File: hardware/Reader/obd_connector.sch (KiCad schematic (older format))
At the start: 1 part, among them CN1 AHDF15A-KG-TAXB

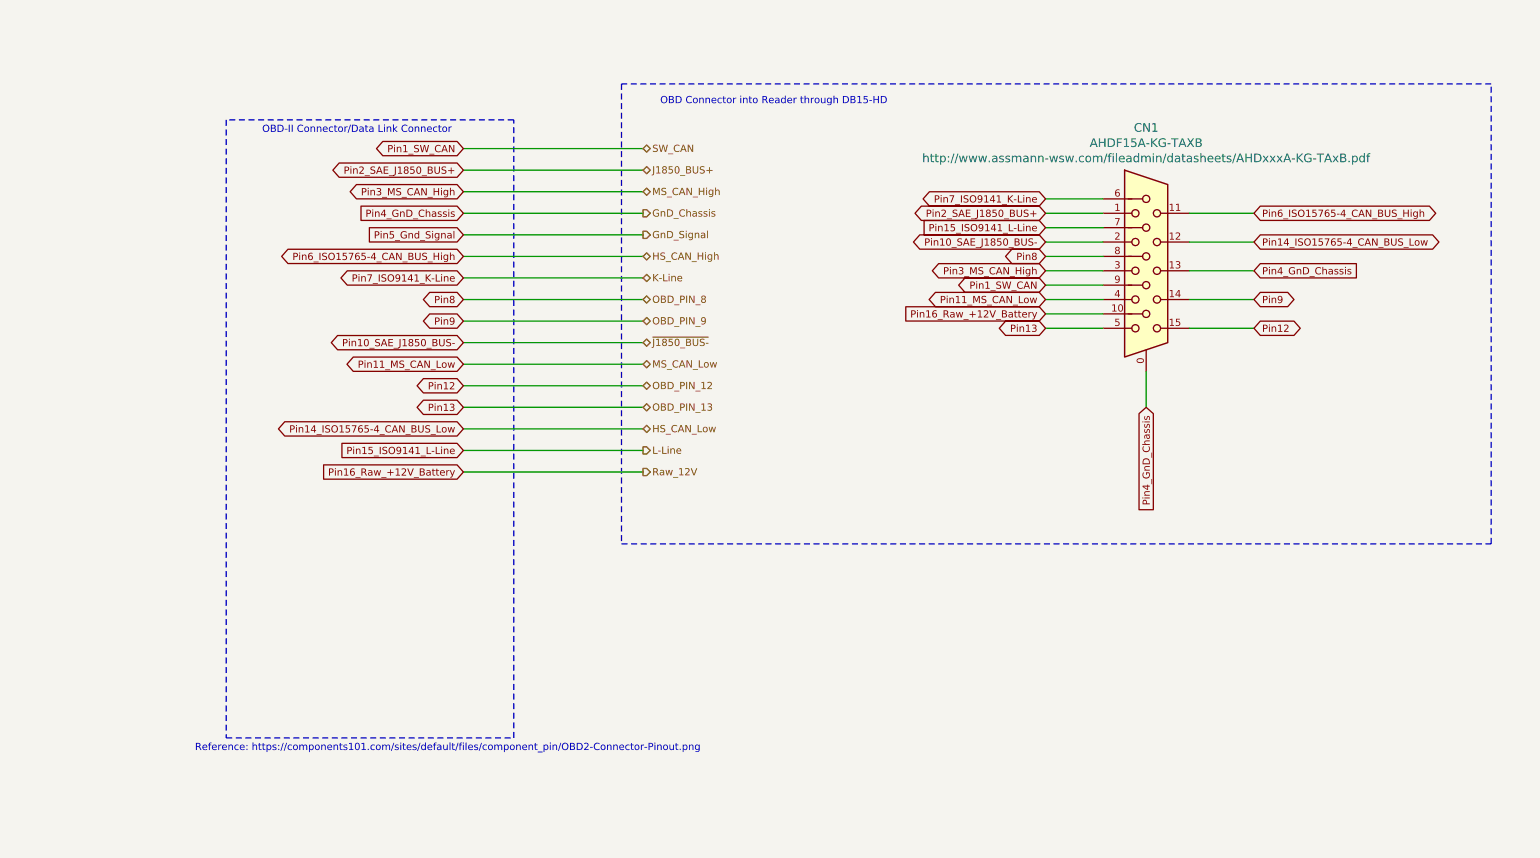
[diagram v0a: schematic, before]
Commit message: Completed Reader schematics for version 0.0.01
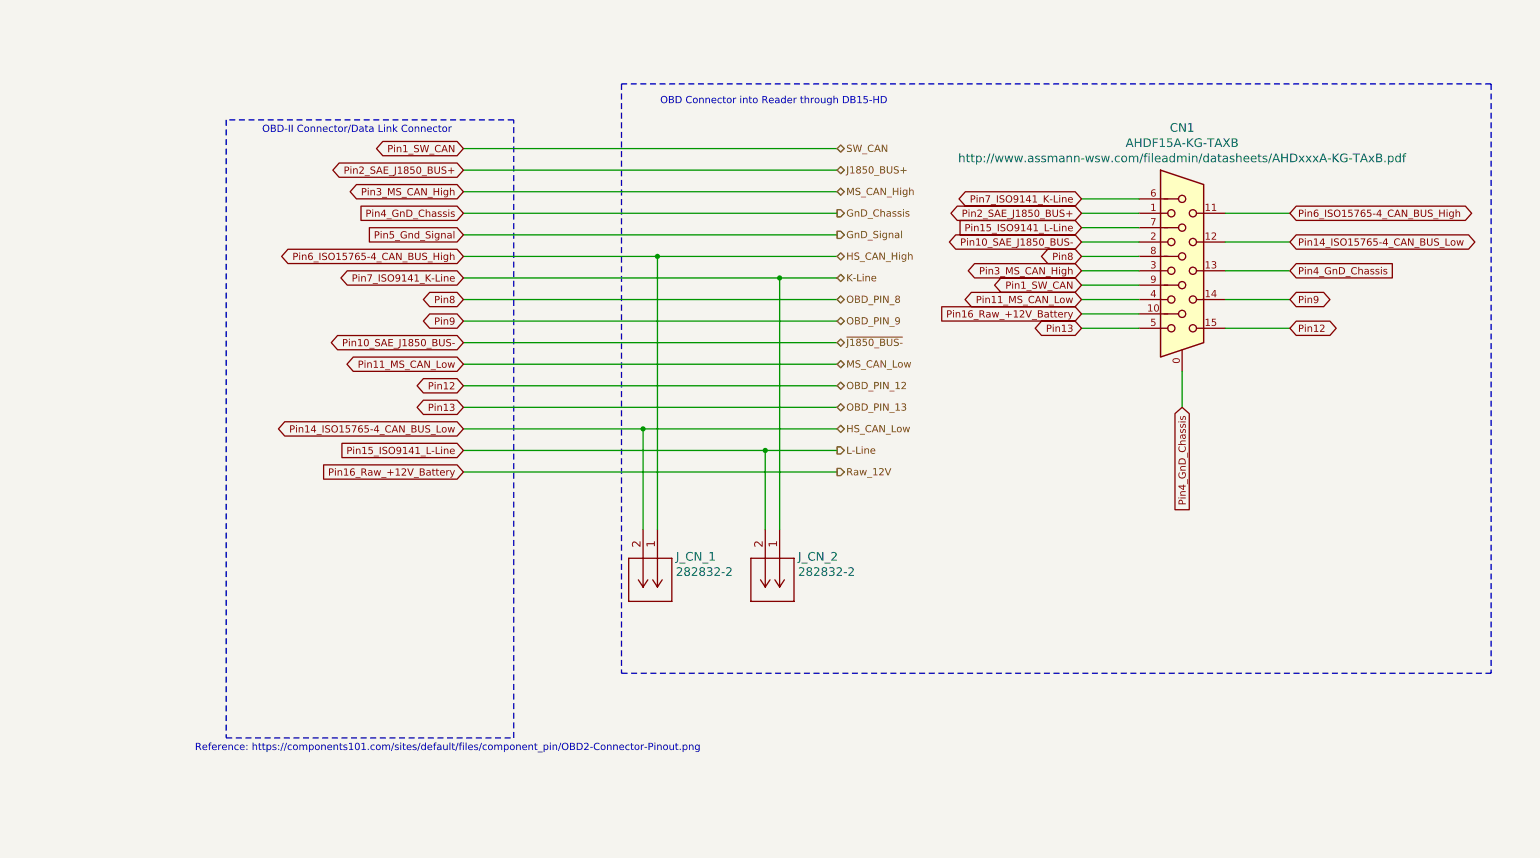
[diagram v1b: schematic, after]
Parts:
- added J_CN_1, J_CN_2: 282832-2, footprints:282832-2, symbol 2828322:282832-2
- CN1: footprint CONN_AHDF15A-KG-TAXB_ASM -> footprints:AHDF15A-KG-TAXB
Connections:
- net Pin14_ISO15765-4_CAN_BUS_Low: now also J_CN_1.2
- net Pin15_ISO9141_L-Line: now also J_CN_2.2
- net Pin6_ISO15765-4_CAN_BUS_High: now also J_CN_1.1
- net Pin7_ISO9141_K-Line: now also J_CN_2.1
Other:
- moved on the sheet: CN1
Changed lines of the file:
@@
 $Descr USLetter 11000 8500
 encoding utf-8
-Sheet 17 17
+Sheet 16 18
 Title "CANnect Reader | OBD Connector"
 Date "2020-10-20"
-Rev "0.0.1"
+Rev "0.0.01"
 Comp "CANtech"
 Comment1 "Created by Choong Jin Ng | jin8383@gmail.com"
 Comment2 "Taken from STN21xx's datasheet for recommended configuration"
 Comment3 ""
-Comment4 "Component Identifier: "
+Comment4 "Component Identifier: CN"
 $EndDescr
 Text GLabel 3000 3800 0    50   Input ~ 0
@@
 Text Notes 1600 1450 0    50   ~ 0
 OBD-II Connector/Data Link Connector
-Text HLabel 4250 1550 2    50   BiDi ~ 0
+Text HLabel 5600 1550 2    50   BiDi ~ 0
 SW_CAN
-Text HLabel 4250 3800 2    50   Output ~ 0
+Text HLabel 5600 3800 2    50   Output ~ 0
 Raw_12V
-Wire Wire Line
-	3000 3800 4250 3800
 Text GLabel 3000 2600 0    50   BiDi ~ 0
 Pin8
-Text HLabel 4250 1700 2    50   BiDi ~ 0
+Text HLabel 5600 1700 2    50   BiDi ~ 0
 J1850_BUS+
-Text HLabel 4250 1850 2    50   BiDi ~ 0
+Text HLabel 5600 1850 2    50   BiDi ~ 0
 MS_CAN_High
-Text HLabel 4250 2000 2    50   Output ~ 0
+Text HLabel 5600 2000 2    50   Output ~ 0
 GnD_Chassis
-Text HLabel 4250 2150 2    50   Output ~ 0
+Text HLabel 5600 2150 2    50   Output ~ 0
 GnD_Signal
-Text HLabel 4250 2300 2    50   BiDi ~ 0
+Text HLabel 5600 2300 2    50   BiDi ~ 0
 HS_CAN_High
-Text HLabel 4250 2450 2    50   BiDi ~ 0
+Text HLabel 5600 2450 2    50   BiDi ~ 0
 K-Line
-Text HLabel 4250 2600 2    50   BiDi ~ 0
+Text HLabel 5600 2600 2    50   BiDi ~ 0
 OBD_PIN_8
-Text HLabel 4250 2750 2    50   BiDi ~ 0
+Text HLabel 5600 2750 2    50   BiDi ~ 0
 OBD_PIN_9
-Text HLabel 4250 2900 2    50   BiDi ~ 0
+Text HLabel 5600 2900 2    50   BiDi ~ 0
 ~J1850_BUS-~
-Text HLabel 4250 3050 2    50   BiDi ~ 0
+Text HLabel 5600 3050 2    50   BiDi ~ 0
 MS_CAN_Low
-Text HLabel 4250 3200 2    50   BiDi ~ 0
+Text HLabel 5600 3200 2    50   BiDi ~ 0
 OBD_PIN_12
-Text HLabel 4250 3350 2    50   BiDi ~ 0
+Text HLabel 5600 3350 2    50   BiDi ~ 0
 OBD_PIN_13
-Text HLabel 4250 3500 2    50   BiDi ~ 0
+Text HLabel 5600 3500 2    50   BiDi ~ 0
 HS_CAN_Low
-Text HLabel 4250 3650 2    50   Output ~ 0
+Text HLabel 5600 3650 2    50   Output ~ 0
 L-Line
-Wire Wire Line
-	3000 1700 4250 1700
-Wire Wire Line
-	3000 1550 4250 1550
-Wire Wire Line
-	3000 1850 4250 1850
-Wire Wire Line
-	3000 2000 4250 2000
-Wire Wire Line
-	3000 2150 4250 2150
-Wire Wire Line
-	3000 2300 4250 2300
-Wire Wire Line
-	3000 2450 4250 2450
-Wire Wire Line
-	3000 2600 4250 2600
-Wire Wire Line
-	3000 2750 4250 2750
-Wire Wire Line
-	3000 2900 4250 2900
-Wire Wire Line
-	3000 3050 4250 3050
-Wire Wire Line
-	3000 3200 4250 3200
-Wire Wire Line
-	3000 3350 4250 3350
-Wire Wire Line
-	3000 3500 4250 3500
-Wire Wire Line
-	3000 3650 4250 3650
 $Comp
 L AHDF15AKGTAXB:AHDF15A-KG-TAXB CN?
 U 1 1 5FF7CC92
-P 7400 1850
+P 7650 1850
 AR Path="/5FF7CC92" Ref="CN?"  Part="1"
 AR Path="/5FF6FE24/5FF7CC92" Ref="CN1"  Part="1"
-F 0 "CN1" H 7750 2295 60  0000 C CNN
-F 1 "AHDF15A-KG-TAXB" H 7750 2189 60  0000 C CNN
-F 2 "CONN_AHDF15A-KG-TAXB_ASM" H 7800 1090 60  0001 C CNN
-F 3 "http://www.assmann-wsw.com/fileadmin/datasheets/AHDxxxA-KG-TAxB.pdf" H 7750 2083 60  0000 C CNN
-	1    7400 1850
+F 0 "CN1" H 8000 2295 60  0000 C CNN
+F 1 "AHDF15A-KG-TAXB" H 8000 2189 60  0000 C CNN
+F 2 "footprints:AHDF15A-KG-TAXB" H 8050 1090 60  0001 C CNN
+F 3 "http://www.assmann-wsw.com/fileadmin/datasheets/AHDxxxA-KG-TAxB.pdf" H 8000 2083 60  0000 C CNN
+	1    7650 1850
 	1    0    0    -1
 $EndComp
-Text GLabel 7050 1900 0    50   BiDi ~ 0
+Text GLabel 7300 1900 0    50   BiDi ~ 0
 Pin7_ISO9141_K-Line
-Text GLabel 7050 2000 0    50   BiDi ~ 0
+Text GLabel 7300 2000 0    50   BiDi ~ 0
 Pin2_SAE_J1850_BUS+
-Text GLabel 7050 2100 0    50   Input ~ 0
+Text GLabel 7300 2100 0    50   Input ~ 0
 Pin15_ISO9141_L-Line
-Text GLabel 7050 2200 0    50   BiDi ~ 0
+Text GLabel 7300 2200 0    50   BiDi ~ 0
 Pin10_SAE_J1850_BUS-
-Text GLabel 7050 2300 0    50   BiDi ~ 0
+Text GLabel 7300 2300 0    50   BiDi ~ 0
 Pin8
-Text GLabel 7050 2400 0    50   BiDi ~ 0
+Text GLabel 7300 2400 0    50   BiDi ~ 0
 Pin3_MS_CAN_High
-Text GLabel 7050 2500 0    50   BiDi ~ 0
+Text GLabel 7300 2500 0    50   BiDi ~ 0
 Pin1_SW_CAN
-Text GLabel 7050 2600 0    50   BiDi ~ 0
+Text GLabel 7300 2600 0    50   BiDi ~ 0
 Pin11_MS_CAN_Low
-Text GLabel 7050 2800 0    50   BiDi ~ 0
+Text GLabel 7300 2800 0    50   BiDi ~ 0
 Pin13
-Text GLabel 7050 2700 0    50   Input ~ 0
+Text GLabel 7300 2700 0    50   Input ~ 0
 Pin16_Raw_+12V_Battery
-Text GLabel 8500 2000 2    50   BiDi ~ 0
+Text GLabel 8750 2000 2    50   BiDi ~ 0
 Pin6_ISO15765-4_CAN_BUS_High
-Text GLabel 8500 2200 2    50   BiDi ~ 0
+Text GLabel 8750 2200 2    50   BiDi ~ 0
 Pin14_ISO15765-4_CAN_BUS_Low
-Text GLabel 8500 2400 2    50   Input ~ 0
+Text GLabel 8750 2400 2    50   Input ~ 0
 Pin4_GnD_Chassis
-Text GLabel 8500 2600 2    50   BiDi ~ 0
+Text GLabel 8750 2600 2    50   BiDi ~ 0
 Pin9
-Text GLabel 8500 2800 2    50   BiDi ~ 0
+Text GLabel 8750 2800 2    50   BiDi ~ 0
 Pin12
-Text GLabel 7750 3350 3    50   Input ~ 0
+Text GLabel 8000 3350 3    50   Input ~ 0
 Pin4_GnD_Chassis
 Wire Wire Line
-	7050 1900 7450 1900
-Wire Wire Line
-	7050 2000 7450 2000
-Wire Wire Line
-	7050 2100 7450 2100
-Wire Wire Line
-	7050 2200 7450 2200
-Wire Wire Line
-	7050 2300 7450 2300
-Wire Wire Line
-	7050 2400 7450 2400
-Wire Wire Line
-	7050 2500 7450 2500
-Wire Wire Line
-	7050 2600 7450 2600
-Wire Wire Line
-	7050 2700 7450 2700
-Wire Wire Line
-	7050 2800 7450 2800
-Wire Wire Line
-	7750 3350 7750 3100
-Wire Wire Line
-	8500 2800 8050 2800
-Wire Wire Line
-	8500 2600 8050 2600
-Wire Wire Line
-	8500 2400 8050 2400
-Wire Wire Line
-	8500 2200 8050 2200
-Wire Wire Line
-	8500 2000 8050 2000
-Wire Notes Line
-	4100 1100 4100 4300
-Wire Notes Line
-	4100 4300 10150 4300
-Wire Notes Line
-	10150 4300 10150 1100
+	7300 1900 7700 1900
+Wire Wire Line
+	7300 2000 7700 2000
+Wire Wire Line
+	7300 2100 7700 2100
+Wire Wire Line
+	7300 2200 7700 2200
+Wire Wire Line
+	7300 2300 7700 2300
+Wire Wire Line
+	7300 2400 7700 2400
+Wire Wire Line
+	7300 2500 7700 2500
+Wire Wire Line
+	7300 2600 7700 2600
+Wire Wire Line
+	7300 2700 7700 2700
+Wire Wire Line
+	7300 2800 7700 2800
+Wire Wire Line
+	8000 3350 8000 3100
+Wire Wire Line
+	8750 2800 8300 2800
+Wire Wire Line
+	8750 2600 8300 2600
+Wire Wire Line
+	8750 2400 8300 2400
+Wire Wire Line
+	8750 2200 8300 2200
+Wire Wire Line
+	8750 2000 8300 2000
 Wire Notes Line
 	10150 1100 4100 1100
@@
 Text Notes 4650 5750 2    50   ~ 0
 Reference: https://components101.com/sites/default/files/component_pin/OBD2-Connector-Pinout.png
+$Comp
+L 2828322:282832-2 J_CN_1
+U 1 1 5F9847E5
+P 4350 4200
+F 0 "J_CN_1" V 4539 4328 60  0000 L CNN
+F 1 "282832-2" V 4645 4328 60  0000 L CNN
+F 2 "footprints:282832-2" H 4750 4140 60  0001 C CNN
+F 3 "https://www.te.com/commerce/DocumentDelivery/DDEController?Action=srchrtrv&DocNm=282832&DocType=Customer+Drawing&DocLang=English" V 4645 4328 60  0001 L CNN
+F 4 "282832-2" H 4350 4200 50  0001 C CNN "Part Name"
+	1    4350 4200
+	0    1    1    0
+$EndComp
+$Comp
+L 2828322:282832-2 J_CN_2
+U 1 1 5F984F05
+P 5200 4200
+F 0 "J_CN_2" V 5389 4328 60  0000 L CNN
+F 1 "282832-2" V 5495 4328 60  0000 L CNN
+F 2 "footprints:282832-2" H 5600 4140 60  0001 C CNN
+F 3 "https://www.te.com/commerce/DocumentDelivery/DDEController?Action=srchrtrv&DocNm=282832&DocType=Customer+Drawing&DocLang=English" V 5495 4328 60  0001 L CNN
+F 4 "282832-2" H 5200 4200 50  0001 C CNN "Part Name"
+	1    5200 4200
+	0    1    1    0
+$EndComp
+Wire Wire Line
+	3000 1550 5600 1550
+Wire Wire Line
+	3000 1700 5600 1700
+Wire Wire Line
+	3000 1850 5600 1850
+Wire Wire Line
+	3000 2000 5600 2000
+Wire Wire Line
+	3000 2150 5600 2150
+Wire Wire Line
+	3000 2300 4350 2300
+Wire Wire Line
+	3000 2600 5600 2600
+Wire Wire Line
+	3000 2750 5600 2750
+Wire Wire Line
+	3000 2900 5600 2900
+Wire Wire Line
+	3000 3050 5600 3050
+Wire Wire Line
+	3000 3200 5600 3200
+Wire Wire Line
+	3000 3350 5600 3350
+Wire Wire Line
+	3000 3500 4250 3500
+Wire Wire Line
+	3000 3650 5100 3650
+Wire Wire Line
+	3000 3800 5600 3800
+Wire Notes Line
+	4100 5200 10150 5200
+Wire Notes Line
+	4100 1100 4100 5200
+Wire Notes Line
+	10150 1100 10150 5200
+Wire Wire Line
+	4250 4200 4250 3500
+Connection ~ 4250 3500
+Wire Wire Line
+	4250 3500 5600 3500
+Wire Wire Line
+	4350 4200 4350 2300
+Connection ~ 4350 2300
+Wire Wire Line
+	4350 2300 5600 2300
+Wire Wire Line
+	5100 4200 5100 3650
+Connection ~ 5100 3650
+Wire Wire Line
+	5100 3650 5600 3650
+Wire Wire Line
+	5200 4200 5200 2450
+Wire Wire Line
+	3000 2450 5200 2450
+Connection ~ 5200 2450
+Wire Wire Line
+	5200 2450 5600 2450
 $EndSCHEMATC

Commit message: Added ESD Protection. Fixed minor bugs on schematic. Attempted placement of components
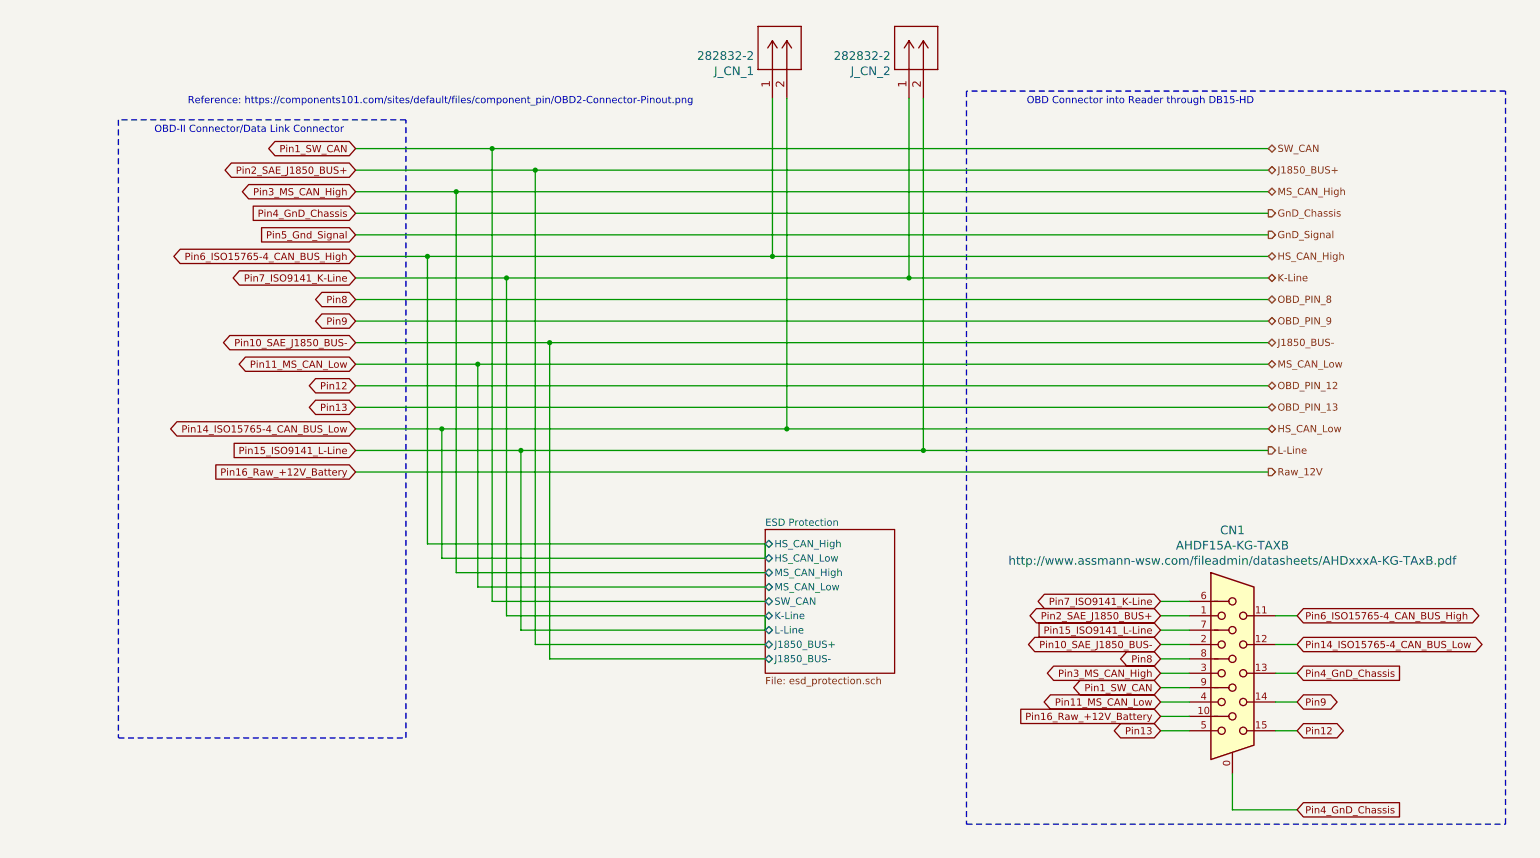
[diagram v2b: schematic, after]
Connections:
- net Pin6_ISO15765-4_CAN_BUS_High is gone; now on net Pin14_ISO15765-4_CAN_BUS_Low: CN1.11, J_CN_1.1
- net Pin7_ISO9141_K-Line is gone; now on net Pin15_ISO9141_L-Line: CN1.6, J_CN_2.1
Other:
- moved on the sheet: CN1, J_CN_1, J_CN_2

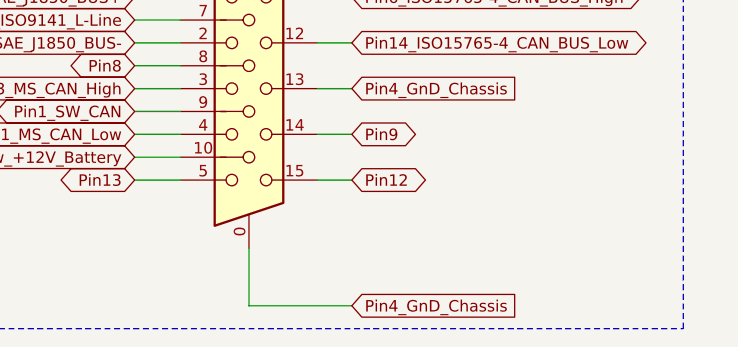
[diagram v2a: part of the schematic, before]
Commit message: Fixed bugs on the reader schematic. Exported Schematic Electrical report
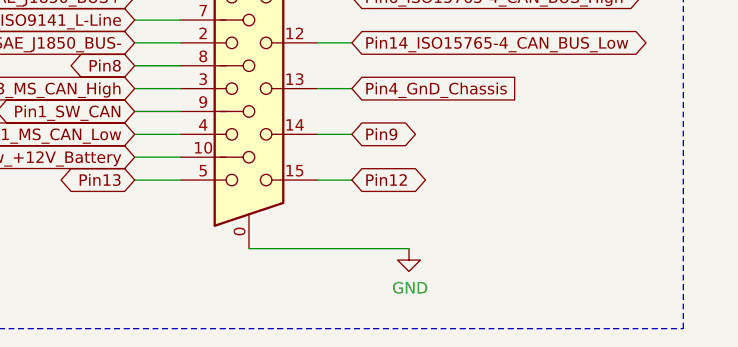
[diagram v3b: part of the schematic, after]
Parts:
- CN1: Manufacturer (none) -> Assmann WSW Components; Part Name (none) -> AHDF15A-KG-TAXB; Vendor (none) -> DigiKey Canada; digikeypn (none) -> AE11024-ND
- J_CN_1, J_CN_2: Manufacturer (none) -> TE Connectivity AMP Connectors; Vendor (none) -> DigiKey Canada; digikeypn (none) -> A113314-ND
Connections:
- net Pin4_GnD_Chassis: no longer CN1.0
- new net GND: CN1.0
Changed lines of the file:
@@
 F 2 "footprints:AHDF15A-KG-TAXB" H 8400 3890 60  0001 C CNN
 F 3 "http://www.assmann-wsw.com/fileadmin/datasheets/AHDxxxA-KG-TAxB.pdf" H 8350 4883 60  0000 C CNN
+F 4 "AHDF15A-KG-TAXB" H 8000 4650 50  0001 C CNN "Part Name"
+F 5 "AE11024-ND" H 8000 4650 50  0001 C CNN "digikeypn"
+F 6 "Assmann WSW Components" H 8000 4650 50  0001 C CNN "Manufacturer"
+F 7 "DigiKey Canada" H 8000 4650 50  0001 C CNN "Vendor"
 	1    8000 4650
 	1    0    0    -1
@@
 Text GLabel 8800 5000 2    50   BiDi ~ 0
 Pin14_ISO15765-4_CAN_BUS_Low
-Text GLabel 8800 5200 2    50   Input ~ 0
-Pin4_GnD_Chassis
 Text GLabel 8800 5400 2    50   BiDi ~ 0
 Pin9
 Text GLabel 8800 5600 2    50   BiDi ~ 0
 Pin12
-Text GLabel 8800 6150 2    50   Input ~ 0
+Text GLabel 8800 5200 2    50   Input ~ 0
 Pin4_GnD_Chassis
-Wire Wire Line
-	8350 6150 8350 5900
 Text Notes 8500 1250 2    50   ~ 0
 OBD Connector into Reader through DB15-HD
@@
 F 3 "https://www.te.com/commerce/DocumentDelivery/DDEController?Action=srchrtrv&DocNm=282832&DocType=Customer+Drawing&DocLang=English" V 5445 1328 60  0001 L CNN
 F 4 "282832-2" H 5150 1200 50  0001 C CNN "Part Name"
+F 5 "DigiKey Canada" H 5150 1200 50  0001 C CNN "Vendor"
+F 6 "TE Connectivity AMP Connectors" H 5150 1200 50  0001 C CNN "Manufacturer"
+F 7 "A113314-ND" H 5150 1200 50  0001 C CNN "digikeypn"
 	1    5150 1200
 	0    -1   -1   0
@@
 F 3 "https://www.te.com/commerce/DocumentDelivery/DDEController?Action=srchrtrv&DocNm=282832&DocType=Customer+Drawing&DocLang=English" V 6395 1328 60  0001 L CNN
 F 4 "282832-2" H 6100 1200 50  0001 C CNN "Part Name"
+F 5 "DigiKey Canada" H 6100 1200 50  0001 C CNN "Vendor"
+F 6 "TE Connectivity AMP Connectors" H 6100 1200 50  0001 C CNN "Manufacturer"
+F 7 "A113314-ND" H 6100 1200 50  0001 C CNN "digikeypn"
 	1    6100 1200
 	0    -1   -1   0
@@
 Pin7_ISO9141_K-Line
 Wire Wire Line
-	8350 6150 8800 6150
-Wire Wire Line
 	8050 5600 7850 5600
 Wire Wire Line
@@
 F10 "J1850_BUS-" B L 5100 5100 50
 $EndSheet
+$Comp
+L power:GND #PWR0103
+U 1 1 5F9F2946
+P 9050 5900
+F 0 "#PWR0103" H 9050 5650 50  0001 C CNN
+F 1 "GND" H 9055 5727 50  0000 C CNN
+F 2 "" H 9050 5900 50  0001 C CNN
+F 3 "" H 9050 5900 50  0001 C CNN
+	1    9050 5900
+	1    0    0    -1
+$EndComp
+Wire Wire Line
+	8350 5900 9050 5900
 $EndSCHEMATC
